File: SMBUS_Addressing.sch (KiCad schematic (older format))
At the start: 15 parts, among them J5 Conn_02x04_Odd_Even, J6 Conn_02x03_Odd_Even, SW1 SW_DIP_x03, U3 4051

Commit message: save
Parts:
- removed J5: Conn_02x04_Odd_Even, Connector_PinHeader_2.54mm:PinHeader_2x04_P2.54mm_Vertical, symbol Connector_Generic:Conn_02x04_Odd_Even
- removed J6: Conn_02x03_Odd_Even, Connector_PinHeader_2.54mm:PinHeader_2x03_P2.54mm_Vertical, symbol Connector_Generic:Conn_02x03_Odd_Even
- added SW2: SW_DIP_x04, Button_Switch_SMD:SW_DIP_SPSTx04_Slide_6.7x11.72mm_W8.61mm_P2.54mm_LowProfile, symbol Switch:SW_DIP_x04
- added SW3: SW_DIP_x03, Button_Switch_SMD:SW_DIP_SPSTx03_Slide_6.7x9.18mm_W8.61mm_P2.54mm_LowProfile, symbol Switch:SW_DIP_x03
- added TP24: TestPoint, TestPoint:TestPoint_Pad_1.0x1.0mm, symbol Connector:TestPoint
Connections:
- net GNDS: now also SW3.4, SW3.5, SW3.6, TP24.1
- net SMBUS_ADDR0: now also SW2.1
- net SMBUS_ADDR1: now also SW2.2
- net SMBUS_ADDR2: now also SW2.3, SW2.4
- net at U3.10 (B): now also SW3.2
- net at U3.11 (A): now also SW3.1
- net at U3.3 (X): now also SW2.5
- net at U3.9 (C): now also SW3.3
- net at R6.2, SW1.1: now also SW2.8
- net at R7.2, SW1.2: now also SW2.7
- net at R8.2, SW1.3: now also SW2.6
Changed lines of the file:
@@
 Wire Wire Line
 	5550 5425 5550 5525
-$Comp
-L Connector_Generic:Conn_02x03_Odd_Even J?
-U 1 1 5F3F82EB
-P 6675 4875
-AR Path="/5EFF0F4B/5F3F82EB" Ref="J?"  Part="1"
-AR Path="/5F02F4E9/5F3E7977/5F3F82EB" Ref="J6"  Part="1"
-AR Path="/5F02F4E9/5F4AA6E5/5F3F82EB" Ref="J6"  Part="1"
-F 0 "J6" H 6725 4650 50  0000 C CNN
-F 1 "Conn_02x03_Odd_Even" H 6725 5101 50  0001 C CNN
-F 2 "Connector_PinHeader_2.54mm:PinHeader_2x03_P2.54mm_Vertical" H 6675 4875 50  0001 C CNN
-F 3 "~" H 6675 4875 50  0001 C CNN
-	1    6675 4875
-	-1   0    0    -1
-$EndComp
 Wire Wire Line
 	6375 4775 6050 4775
@@
 $EndComp
 Wire Wire Line
-	7300 4975 6875 4975
-Wire Wire Line
-	6875 4875 7300 4875
+	7300 4975 6975 4975
+Wire Wire Line
+	6975 4875 7300 4875
 Wire Wire Line
 	7300 4875 7300 4975
@@
 	7300 4975 7300 5525
 Wire Wire Line
-	6875 4775 7300 4775
+	6975 4775 7300 4775
 Wire Wire Line
 	7300 4775 7300 4875
 Connection ~ 7300 4875
-Wire Wire Line
-	7300 4775 7300 4675
-Wire Wire Line
-	7300 4675 6050 4675
 Connection ~ 7300 4775
 $Comp
@@
 Wire Wire Line
 	7300 3775 7300 3875
-Connection ~ 7300 4675
 Connection ~ 7300 3875
 Wire Wire Line
@@
 	7300 4375 7300 4475
 Connection ~ 7300 4475
-Wire Wire Line
-	7300 4475 7300 4675
-Text HLabel 2750 3225 0    50   Input ~ 0
+Text HLabel 2650 3225 0    50   Input ~ 0
 SMBUS_ADDR2
-Text HLabel 2750 3125 0    50   Input ~ 0
+Text HLabel 2650 3125 0    50   Input ~ 0
 SMBUS_ADDR1
-Text HLabel 2750 3025 0    50   Input ~ 0
+Text HLabel 2650 3025 0    50   Input ~ 0
 SMBUS_ADDR0
 Text HLabel 5550 3375 1    50   Input ~ 0
@@
 Wire Wire Line
 	5550 3375 5550 3475
-$Comp
-L Connector_Generic:Conn_02x04_Odd_Even J5
-U 1 1 5F4489DA
-P 3150 3125
-AR Path="/5F02F4E9/5F3E7977/5F4489DA" Ref="J5"  Part="1"
-AR Path="/5F02F4E9/5F4AA6E5/5F4489DA" Ref="J5"  Part="1"
-F 0 "J5" H 3200 3350 50  0000 C CNN
-F 1 "Conn_02x04_Odd_Even" H 3200 3351 50  0001 C CNN
-F 2 "Connector_PinHeader_2.54mm:PinHeader_2x04_P2.54mm_Vertical" H 3150 3125 50  0001 C CNN
-F 3 "~" H 3150 3125 50  0001 C CNN
-	1    3150 3125
-	1    0    0    -1
-$EndComp
-Wire Wire Line
-	2750 3025 2950 3025
-Wire Wire Line
-	2750 3125 2950 3125
+Wire Wire Line
+	2650 3025 2850 3025
+Wire Wire Line
+	2650 3125 2850 3125
+Wire Wire Line
+	2650 3225 2750 3225
+Wire Wire Line
+	2850 3325 2750 3325
+Wire Wire Line
+	2750 3325 2750 3225
+Connection ~ 2750 3225
 Wire Wire Line
 	2750 3225 2850 3225
-Wire Wire Line
-	2950 3325 2850 3325
-Wire Wire Line
-	2850 3325 2850 3225
-Connection ~ 2850 3225
-Wire Wire Line
-	2850 3225 2950 3225
 Wire Wire Line
 	3450 3325 3875 3325
@@
 	-1   0    0    -1
 $EndComp
+$Comp
+L Switch:SW_DIP_x04 SW2
+U 1 1 5F2ADDB0
+P 3150 3225
+F 0 "SW2" H 3150 3692 50  0000 C CNN
+F 1 "SW_DIP_x04" H 3150 3601 50  0000 C CNN
+F 2 "Button_Switch_SMD:SW_DIP_SPSTx04_Slide_6.7x11.72mm_W8.61mm_P2.54mm_LowProfile" H 3150 3225 50  0001 C CNN
+F 3 "~" H 3150 3225 50  0001 C CNN
+	1    3150 3225
+	1    0    0    -1
+$EndComp
+Wire Wire Line
+	6050 4675 6325 4675
+Wire Wire Line
+	6325 4675 6325 4625
+$Comp
+L Switch:SW_DIP_x03 SW3
+U 1 1 5F2BCE96
+P 6675 4975
+F 0 "SW3" H 6675 4800 50  0000 C CNN
+F 1 "SW_DIP_x03" H 6675 4700 50  0000 C CNN
+F 2 "Button_Switch_SMD:SW_DIP_SPSTx03_Slide_6.7x9.18mm_W8.61mm_P2.54mm_LowProfile" H 6675 4975 50  0001 C CNN
+F 3 "~" H 6675 4975 50  0001 C CNN
+	1    6675 4975
+	1    0    0    -1
+$EndComp
+Wire Wire Line
+	7300 4475 7300 4625
+Wire Wire Line
+	6325 4625 7300 4625
+Connection ~ 7300 4625
+Wire Wire Line
+	7300 4625 7300 4775
+$Comp
+L Connector:TestPoint TP?
+U 1 1 5F341E88
+P 3125 3900
+AR Path="/5F02F4E9/5F341E88" Ref="TP?"  Part="1"
+AR Path="/5F02F4E9/5F4AA6E5/5F341E88" Ref="TP24"  Part="1"
+F 0 "TP24" H 3183 4018 50  0000 L CNN
+F 1 "TestPoint" H 3183 3927 50  0000 L CNN
+F 2 "TestPoint:TestPoint_Pad_1.0x1.0mm" H 3325 3900 50  0001 C CNN
+F 3 "~" H 3325 3900 50  0001 C CNN
+	1    3125 3900
+	1    0    0    -1
+$EndComp
+Wire Wire Line
+	3125 3900 3125 4150
+$Comp
+L power:GNDS #PWR017
+U 1 1 5F344131
+P 3125 4150
+F 0 "#PWR017" H 3125 3900 50  0001 C CNN
+F 1 "GNDS" H 3130 3977 50  0000 C CNN
+F 2 "" H 3125 4150 50  0001 C CNN
+F 3 "" H 3125 4150 50  0001 C CNN
+	1    3125 4150
+	1    0    0    -1
+$EndComp
 $EndSCHEMATC

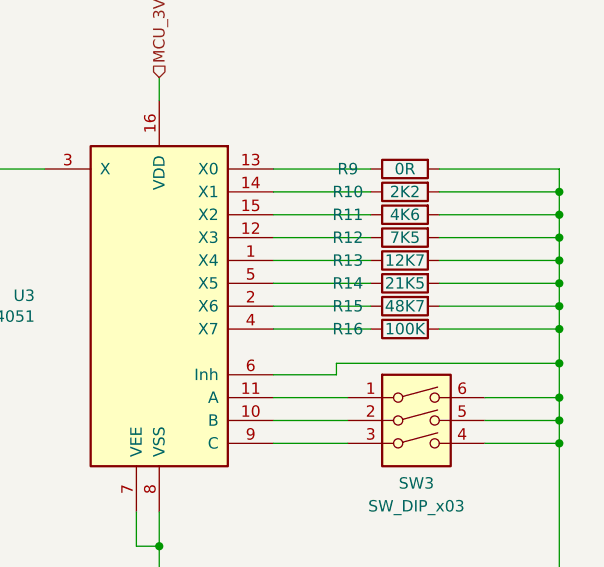
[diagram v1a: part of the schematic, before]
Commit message: updates
set U3 4051 address resistors to E12 values
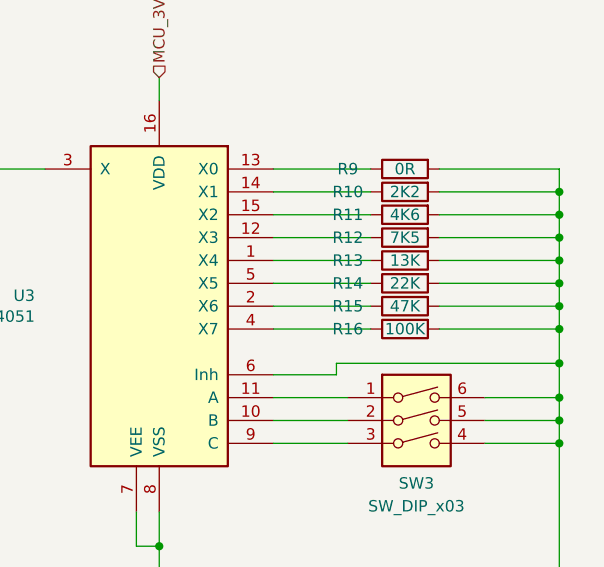
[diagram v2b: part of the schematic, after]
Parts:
- R13: value 12K7 -> 13K
- R14: value 21K5 -> 22K
- R15: value 48K7 -> 47K
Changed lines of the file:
@@
 AR Path="/5F02F4E9/5F4AA6E5/5F3F830D" Ref="R15"  Part="1"
 F 0 "R15" V 6625 4625 50  0000 C CNN
-F 1 "48K7" V 6625 4375 50  0000 C CNN
+F 1 "47K" V 6625 4375 50  0000 C CNN
 F 2 "Resistor_SMD:R_0805_2012Metric_Pad1.15x1.40mm_HandSolder" V 6555 4375 50  0001 C CNN
 F 3 "~" H 6625 4375 50  0001 C CNN
@@
 AR Path="/5F02F4E9/5F4AA6E5/5F3F8315" Ref="R14"  Part="1"
 F 0 "R14" V 6625 4525 50  0000 C CNN
-F 1 "21K5" V 6625 4275 50  0000 C CNN
+F 1 "22K" V 6625 4275 50  0000 C CNN
 F 2 "Resistor_SMD:R_0805_2012Metric_Pad1.15x1.40mm_HandSolder" V 6555 4275 50  0001 C CNN
 F 3 "~" H 6625 4275 50  0001 C CNN
@@
 AR Path="/5F02F4E9/5F4AA6E5/5F3F831D" Ref="R13"  Part="1"
 F 0 "R13" V 6625 4425 50  0000 C CNN
-F 1 "12K7" V 6625 4175 50  0000 C CNN
+F 1 "13K" V 6625 4175 50  0000 C CNN
 F 2 "Resistor_SMD:R_0805_2012Metric_Pad1.15x1.40mm_HandSolder" V 6555 4175 50  0001 C CNN
 F 3 "~" H 6625 4175 50  0001 C CNN
